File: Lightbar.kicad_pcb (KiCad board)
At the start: 2 copper layers, 100 x 14 mm, 17 parts, among them IC1 PAM2863ECR, IC2 PAM2863ECR, J1 Conn_01x04_Pin

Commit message: updated lightbar
added resistors and transistor
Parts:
- added Q1: 2N2219, Package_TO_SOT_SMD:SC-59_Handsoldering, F.Cu at (149.0, 100.5)
- added R3: R_US, Resistor_SMD:R_0805_2012Metric_Pad1.20x1.40mm_HandSolder, F.Cu at (160.0, 99.0)
- added R4: R_US, Resistor_SMD:R_0805_2012Metric_Pad1.20x1.40mm_HandSolder, F.Cu at (155.0, 99.0)
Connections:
- J1 pad 1: N$4 -> Net-(D1-K)
- J1 pad 2: PWM1 -> Net-(IC2-VSET)
- J1 pad 3: N$10 -> Net-(J1-Pin_3)
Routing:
- net Net-(D1-K): track 0.00 -> 22.5 mm, vias 0 -> 2
- net Net-(J1-Pin_3): track 0.00 -> 13.1 mm, vias 0 -> 2
- net Net-(Q1-E): track 0.00 -> 10.9 mm, vias 0 -> 2
- net GND: track 204.0 -> 202.9 mm
- net PWM1: track 43.3 -> 44.0 mm

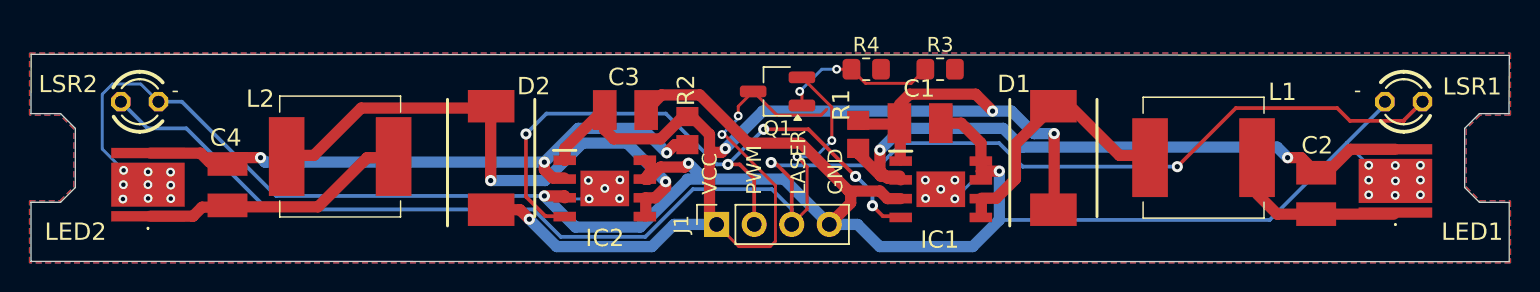
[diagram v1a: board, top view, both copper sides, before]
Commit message: reworked laser system
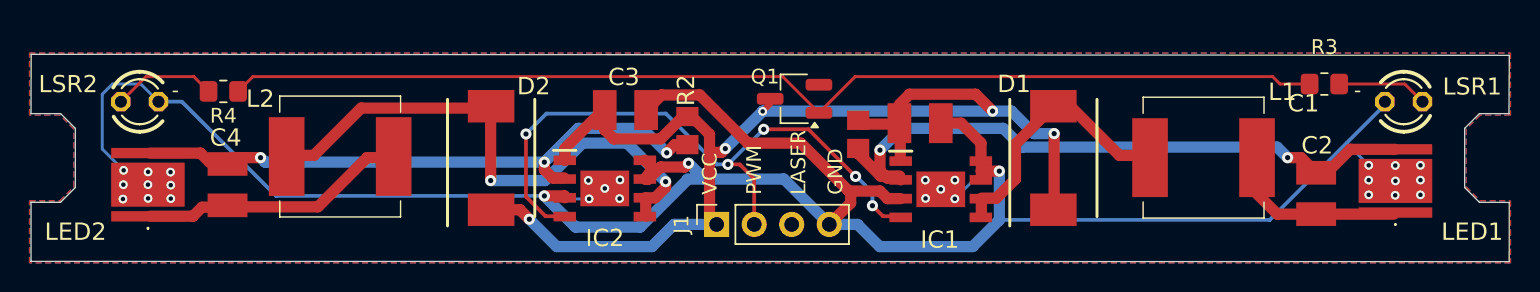
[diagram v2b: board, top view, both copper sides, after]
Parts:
- moved R4 43.5 mm to (111.5, 100.5), turned to 180 degrees
- moved R3 26.0 mm to (186.0, 100.0)
- moved Q1 1.25 mm to (150.2, 101.0)
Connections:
- J1 pad 1: Net-(D1-K) -> N$4
- LSR1 pad A: N$10 -> Net-(LASER1-PadA)
- LSR2 pad A: N$10 -> Net-(LASER2-PadA)
- Q1 pad 3: Net-(D1-K) -> N$4
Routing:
- net N$10: track 105.0 -> 0.00 mm, vias 2 -> 0
- net Net-(Q1-E): track 10.9 -> 75.2 mm, vias 2 -> 0
- net Net-(D1-K): track 22.5 -> 0.00 mm, vias 2 -> 0
- net Net-(J1-Pin_3): track 13.1 -> 0.38 mm, vias 2 -> 0
- net Net-(LASER2-PadA): track 0.00 -> 7.05 mm
- net Net-(LASER1-PadA): track 0.00 -> 6.13 mm
- net N$4: track 81.7 -> 82.9 mm, vias 4 -> 5

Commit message: Create Final Gerber Finals
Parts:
- moved R4 0.50 mm to (111.5, 100.0)
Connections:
- J1 pad 2: Net-(IC2-VSET) -> PWM1
- J1 pad 3: Net-(J1-Pin_3) -> Net-(Q1-E)
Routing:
- net Net-(Q1-E): track 75.2 -> 86.0 mm, vias 0 -> 2
- net GND: track 202.9 -> 198.1 mm
